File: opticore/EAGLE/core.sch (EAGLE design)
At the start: 67 parts, among them IC2 MC33269T-5.0, J1 POWER_JACKSLT, Q1 2N3904, Q2 2N3904, Q3 2N3904, Q4 2N3904, Q5 2N3904, Q6 2N3904, Q7 2N3904, X1 FFKV8

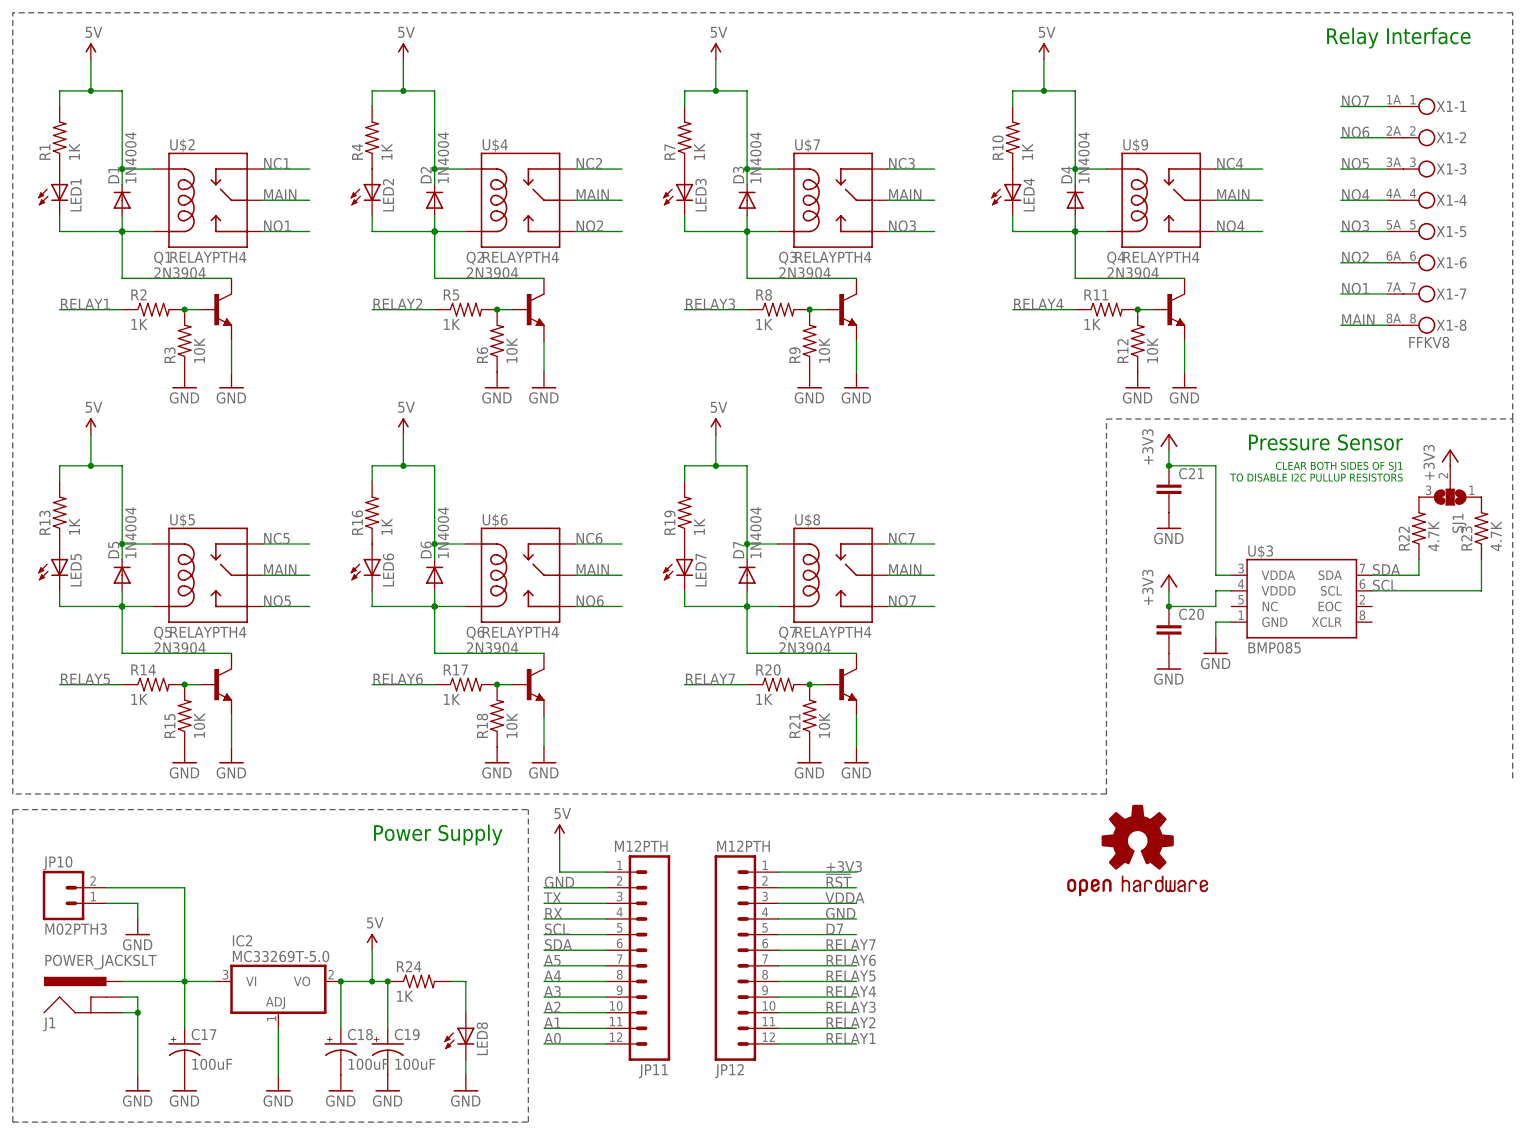
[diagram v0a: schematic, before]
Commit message: Redoing power supply section
This isn't done yet. I still have to connect the 24VAC to the solenoids.
All GND pins on solenoids are tied together then to COMMON.
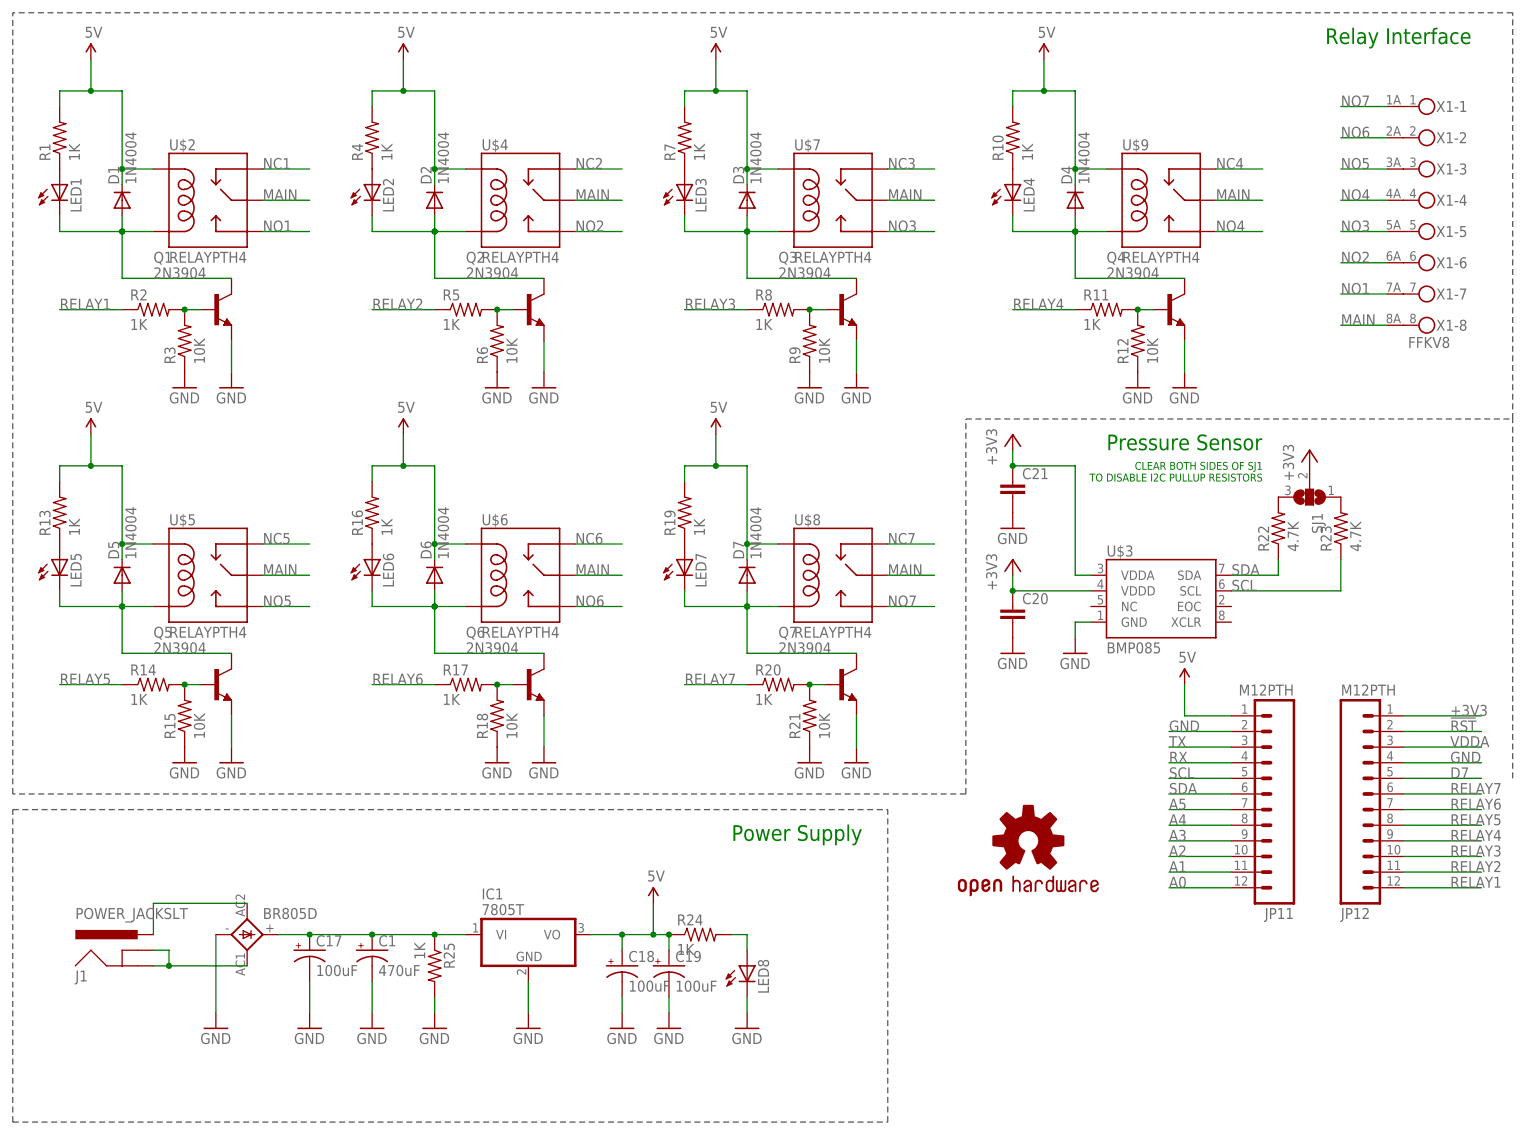
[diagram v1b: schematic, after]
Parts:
- removed IC2: MC33269T-5.0, linear:MC33269T-5.0
- removed JP10: M02PTH3, SparkFun-Connectors:M02PTH3
- added BR805D: (no value), rectifier:GBU4S
- added C1: 470uF, SparkFun-Passives:CAP_POLPTH1
- added IC1: 7805T, adafruit:7805T
- added R25: 1K, SparkFun-Resistors:RESISTORAXIAL-0.3
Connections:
- removed net N$37: C17.+, IC2.VI, J1.PWR, JP10.2
- new net 24VAC+: BR805D.AC2, J1.GND, J1.GNDBREAK
- new net 24VAC-: BR805D.AC1, J1.PWR
- new net N$13: BR805D.+, C1.+, C17.+, IC1.VI, R25.1
- net 5V: now also IC1.VO; no longer IC2.VO
- net GND: now also BR805D.-, C1.-, IC1.GND, R25.2; no longer IC2.ADJ, J1.GND, J1.GNDBREAK, JP10.1
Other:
- moved on the sheet: C17, C18, C19, C20, C21, J1, JP11, JP12, LED8, R22, R23, R24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
